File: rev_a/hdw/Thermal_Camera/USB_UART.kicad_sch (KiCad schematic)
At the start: 37 parts, among them U1303 74LVC1G97, U1304 ISO7321C

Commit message: added PIC32 bypass, SD card load switch, other random junk
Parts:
- removed C? (x2): 0.1uF, Capacitors_SMD:C_0603, symbol Custom_Library:C_Custom
- removed D?: Green, LEDs:LED_0603, symbol Device:LED
- removed J?: USB_B_Mini, Connectors:USB_Mini-B, symbol Connector:USB_B_Mini
- removed L? (x2): 600R 0.5A, Inductors_SMD:L_0603, symbol Device:Ferrite_Bead
- removed R? (x4): 100k, Resistors_SMD:R_0603, symbol Custom_Library:R_Custom
- removed R?: 1k, Resistors_SMD:R_0603, symbol Custom_Library:R_Custom
- removed TP?: TP, Custom Footprints Library:Test_Point, symbol Custom_Library:TP
- removed U1303: 74LVC1G97, Package_TO_SOT_SMD:SOT-363_SC-70-6, symbol Custom Library:74LVC1G97_Power_NOT
- removed U1304: ISO7321C, Package_SO:SOIC-8_3.9x4.9mm_P1.27mm, symbol Isolator:ISO7321C
- removed U?: TPD3S014DBVR, TO_SOT_Packages_SMD:SOT-23-6, symbol Custom_Library:TPD3S014DBVR
- added C?: 0.1uF, Capacitors_SMD:C_0603, symbol Custom_Library:C_Custom
- added R?: 10k, Resistors_SMD:R_0603, symbol Custom_Library:R_Custom
- added R? (x2): 15k, Resistors_SMD:R_0603, symbol Custom_Library:R_Custom
- added U?: FXMA108, Package_DFN_QFN:WQFN-20-1EP_2.5x4.5mm_P0.5mm_EP1x2.9mm, symbol Logic_LevelTranslator:FXMA108
- added U?: 74LVC1G97, Package_TO_SOT_SMD:SOT-363_SC-70-6, symbol Custom Library:74LVC1G97_Power_NOT
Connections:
- net GND_USB is gone; now on net GND: C?.2, C?.2, C?.2, C?.2, C?.2, C?.2, C?.2, C?.2, C?.2, R?.2, U?.13 (GND), U?.2 (GND), U?.5 (GND)
- net +3.3V_USB: now also U?.20 (VCCB); no longer C?.1, R?.1, U?.5 (Vs)
- net GND: now also C?.2, R?.2, R?.2, U?.10 (GND), U?.2 (GND), U?.3 (GND)
- net USB_UART_RX: now also U?.2 (A0)
- net USB_UART_TX: now also U?.3 (A1)
- net ~{USB_UART_CTS_BUF}: now reaches U?.11 (~{CTS})
- net ~{USB_UART_CTS_BUF}: now also U?.16 (B3)
- net ~{USB_UART_RTS_BUF}: now reaches U?.8 (~{RTS})
- net ~{USB_UART_RTS_BUF}: now also U?.17 (B2)
- net +3.3V renamed +3.0V
- net +3.0V: now also C?.1, R?.1, U?.5 (Vs), C?.1, R?.1, U?.1 (VCC), U?.1 (VCCA), U?.5 (VCC)
- net CONN_USB+ renamed BRIDGE_USB_D+
- net BRIDGE_USB_D+: now also R?.1
- net CONN_USB- renamed BRIDGE_USB_D-
- net BRIDGE_USB_D-: now also R?.1
- net USB_UART_RX_ISO renamed USB_UART_RX_BUF
- net USB_UART_RX_BUF: now also U?.19 (B0)
- net USB_UART_TX_ISO renamed USB_UART_TX_BUF
- net USB_UART_TX_BUF: now also U?.18 (B1)
- new net: R?.2, U?.11 (~{OE}), U?.4
- new net POS3P0_PGOOD: U?.6
- new net ~{USB_UART_CTS}: U?.5 (A3)
- new net ~{USB_UART_RTS}: U?.4 (A2)
- no-connect marks 4 -> 9
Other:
- note added: "CONSIDER SERIAL BRIDGE WITH LARGER BUFFER"
- note added: "FXMA108 recommends no pull resistors"
- note removed: "CHANGE TO NON-ISOLATED CONSIDER SERIAL BRIDGE WITH LARGER BUFFER CONSIDER HARDWARE FLOW CONTROL"
- moved on the sheet: C?

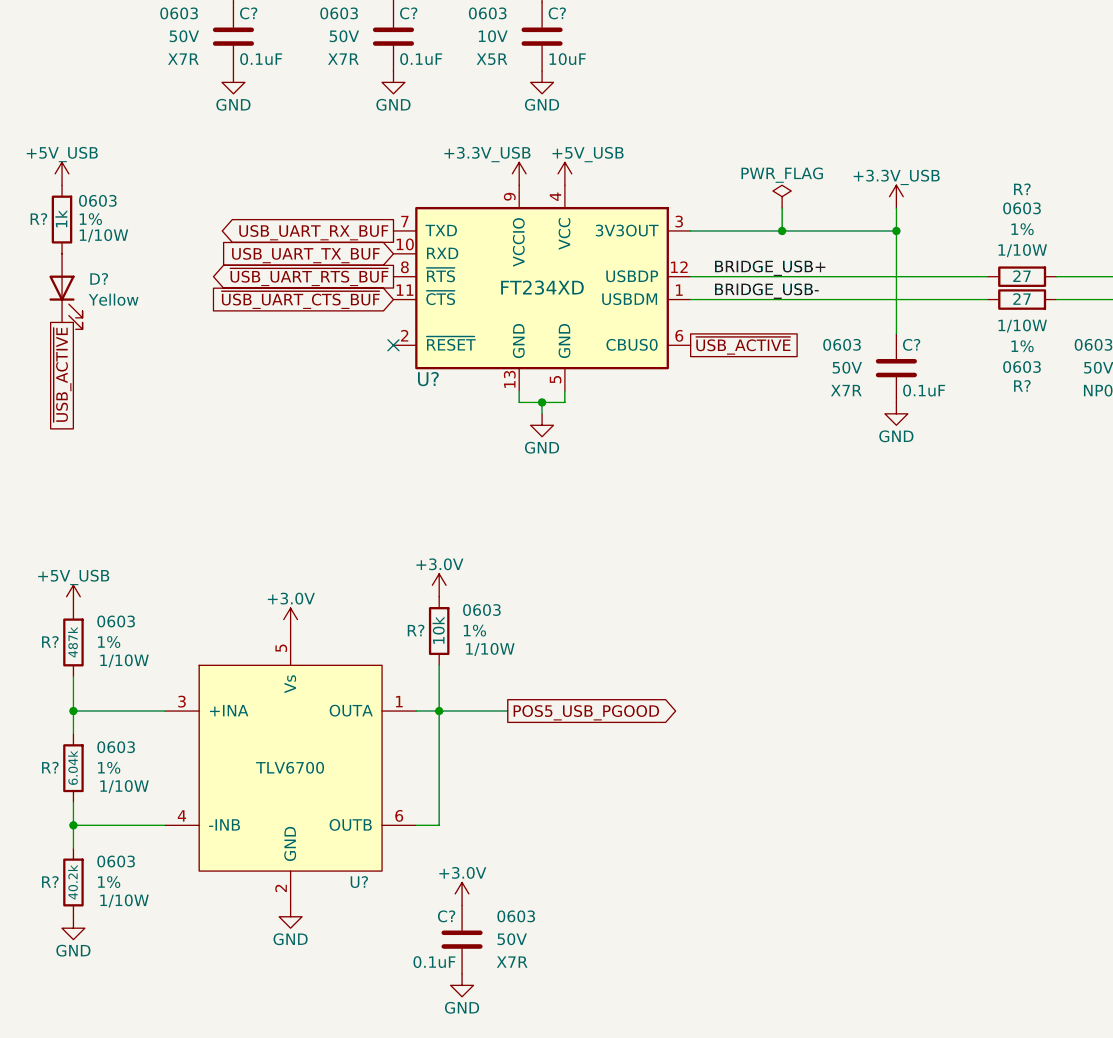
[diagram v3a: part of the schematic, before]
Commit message: added some USB stuff
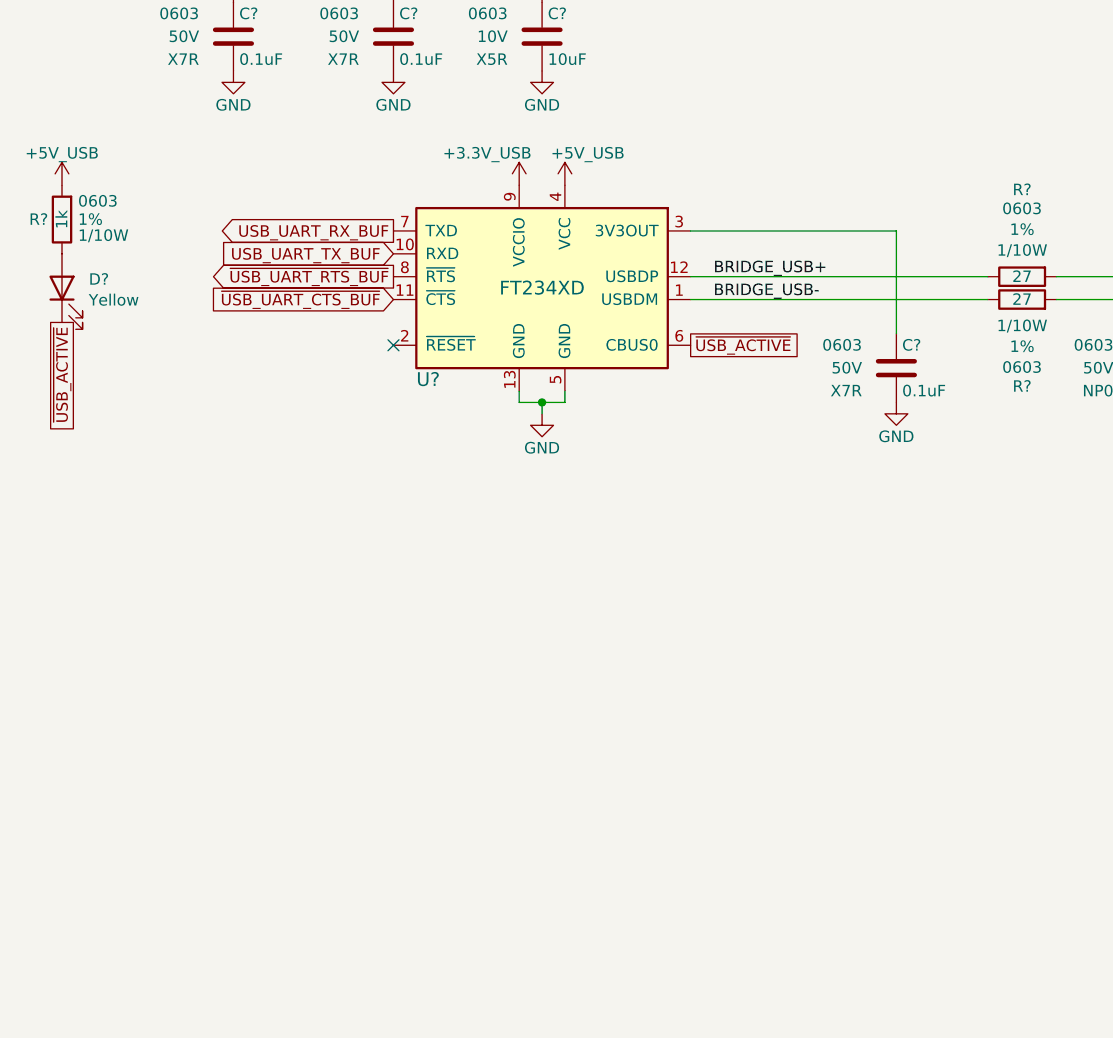
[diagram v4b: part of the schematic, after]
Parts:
- removed C?: 0.1uF, Capacitors_SMD:C_0603, symbol Custom_Library:C_Custom
- removed R?: 10k, Resistors_SMD:R_0603, symbol Custom_Library:R_Custom
- removed R?: 6.04k, Resistors_SMD:R_0603, symbol Custom_Library:R_Custom
- removed R?: 40.2k, Resistors_SMD:R_0603, symbol Custom_Library:R_Custom
- removed R?: 487k, Resistors_SMD:R_0603, symbol Custom_Library:R_Custom
- removed U?: TLV6700, Package_TO_SOT_SMD:SOT-23-6, symbol Custom_Library:TLV6700
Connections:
- net +3.3V_USB: no longer C?.1, U?.3 (3V3OUT)
- new net: C?.1, U?.3 (3V3OUT)

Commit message: added some more USB stuff
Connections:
- net POS3P3_USB_PGOOD: now reaches U?.2 (~{RESET})
- no-connect marks 9 -> 8
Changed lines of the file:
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@@
   (no_connect (at 144.78 55.88))
   (no_connect (at 144.78 48.26))
-  (no_connect (at 62.23 118.11))
   (no_connect (at 124.46 48.26))
   (no_connect (at 124.46 55.88))
@@
       (effects (font (size 1.27 1.27)) (justify right) hide)
     )
+  )
+  (global_label "POS3P3_USB_PGOOD" (shape input) (at 62.23 118.11 180) (fields_autoplaced)
+    (effects (font (size 1.27 1.27)) (justify right))
+    (property "Intersheetrefs" "${INTERSHEET_REFS}" (at 39.609 118.11 0)
+      (effects (font (size 1.27 1.27)) (justify right) hide)
+    )

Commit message: lots of random schematic progress
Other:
- note removed: "CONSIDER SERIAL BRIDGE WITH LARGER BUFFER"
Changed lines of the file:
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@@
     (effects (font (size 1.27 1.27)) (justify left bottom))
-  )
-  (text "CONSIDER SERIAL BRIDGE WITH\nLARGER BUFFER" (at 144.78 170.18 0)
-    (effects (font (face "Courier New") (size 5.08 5.08) (thickness 1.016) bold (color 194 0 0 1)) (justify left bottom))
   )
   (label "BRIDGE_USB+" (at 97.79 110.49 0) (fields_autoplaced)
